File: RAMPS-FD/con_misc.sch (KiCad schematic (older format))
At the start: 15 parts, among them K201 S1, K202 S2, K203 S3, K204 S4, P1 SERIAL1, P2 I2C-1, P211 I2C-0, P213 AUX-4, P214 AUX-2, P215 AUX-3, P216 SERIAL0

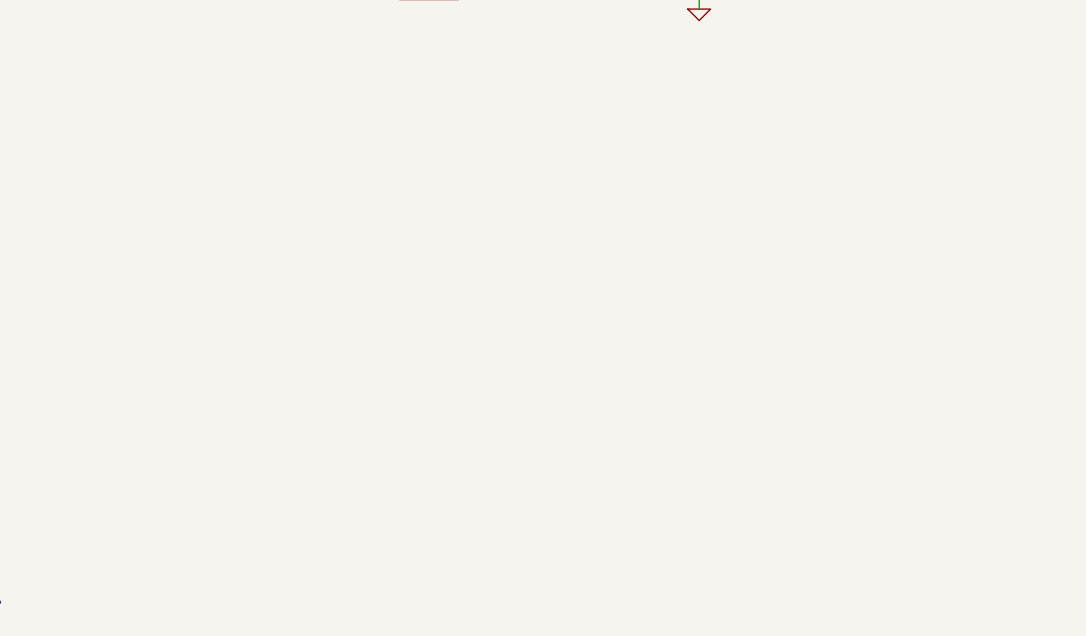
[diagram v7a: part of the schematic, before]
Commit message: RAMPS-FD schematic changes: #3 replace C301, C302, C303 and C501 with ceramic 0805; #4 change endstop connectors to 6x1 and 6x2 to allow key position #9 change E-STOP connector to KK type; #18 add 10k pulldowns on heater outputs from CPU #19 change E-STOP buffers to HCT type to always drive FETs at 5V and remove inverting drivers on heater outputs; #20 add 24LC256 I2C EEPROM
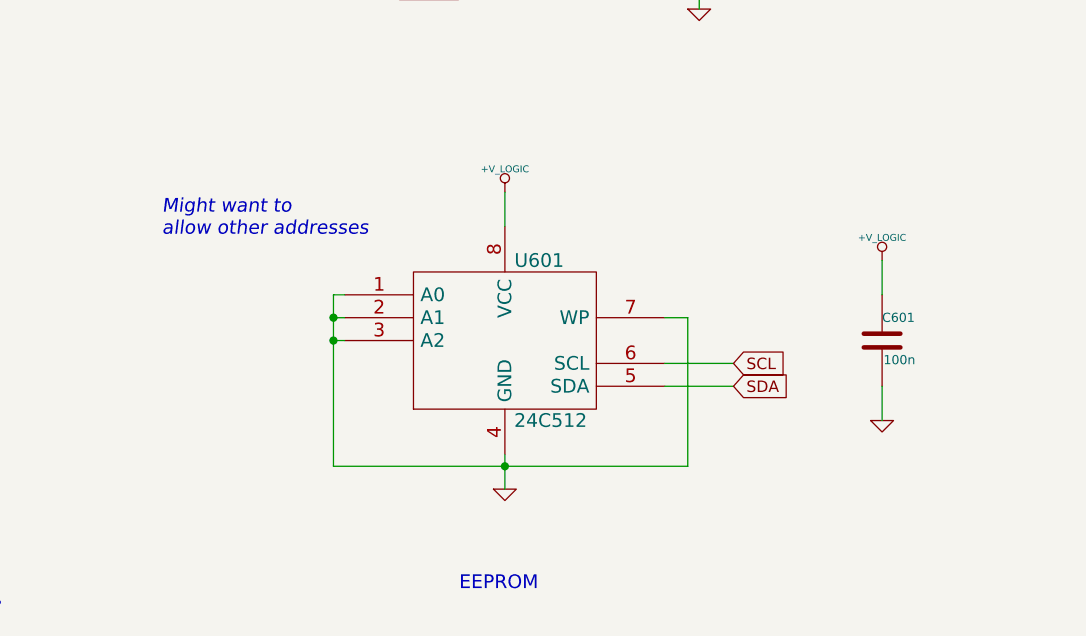
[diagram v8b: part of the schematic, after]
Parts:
- added C601: 100n, ~, symbol C
- added U601: 24C512, symbol 24C512
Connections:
- net +V_LOGIC: now also C601.1, U601.8 (VCC)
- net GND: now also C601.2, U601.1 (A0), U601.2 (A1), U601.3 (A2), U601.4 (GND), U601.7 (WP)
- net SCL: now also U601.6 (SCL)
- net SDA: now also U601.5 (SDA)
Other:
- note added: "EEPROM"
- note added: "Might want to \nallow other addresses"
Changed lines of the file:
@@
 Sheet 6 9
 Title ""
-Date "6 oct 2013"
+Date "18 dec 2013"
 Rev "0.2"
 Comp ""
@@
 $EndComp
 $Comp
-L GND #PWR065
+L GND #PWR067
 U 1 1 523B601D
 P 5250 4800
-F 0 "#PWR065" H 5250 4800 30  0001 C CNN
+F 0 "#PWR067" H 5250 4800 30  0001 C CNN
 F 1 "GND" H 5250 4730 30  0001 C CNN
 F 2 "" H 5250 4800 60  0001 C CNN
@@
 SCL1
 $Comp
-L +V_LOGIC #PWR066
+L +V_LOGIC #PWR068
 U 1 1 523B601C
 P 4450 3800
-F 0 "#PWR066" H 4450 3770 30  0001 C CNN
+F 0 "#PWR068" H 4450 3770 30  0001 C CNN
 F 1 "+V_LOGIC" H 4450 3900 30  0000 C CNN
 F 2 "" H 4450 3800 60  0001 C CNN
@@
 UART1_TX_LV
 $Comp
-L GND #PWR067
+L GND #PWR069
 U 1 1 523B5AB9
 P 1950 3600
-F 0 "#PWR067" H 1950 3600 30  0001 C CNN
+F 0 "#PWR069" H 1950 3600 30  0001 C CNN
 F 1 "GND" H 1950 3530 30  0001 C CNN
 F 2 "" H 1950 3600 60  0001 C CNN
@@
 D51-MOSI
 $Comp
-L +V_LOGIC #PWR068
+L +V_LOGIC #PWR070
 U 1 1 517867DD
 P 7950 1750
-F 0 "#PWR068" H 7950 1720 30  0001 C CNN
+F 0 "#PWR070" H 7950 1720 30  0001 C CNN
 F 1 "+V_LOGIC" H 7950 1850 30  0000 C CNN
 F 2 "" H 7950 1750 60  0001 C CNN
@@
 $EndComp
 $Comp
-L +V_LOGIC #PWR069
+L +V_LOGIC #PWR071
 U 1 1 517867D0
 P 8250 6850
-F 0 "#PWR069" H 8250 6820 30  0001 C CNN
+F 0 "#PWR071" H 8250 6820 30  0001 C CNN
 F 1 "+V_LOGIC" H 8250 6950 30  0000 C CNN
 F 2 "" H 8250 6850 60  0001 C CNN
@@
 $EndComp
 $Comp
-L +V_LOGIC #PWR070
+L +V_LOGIC #PWR072
 U 1 1 517867C6
 P 4450 1600
-F 0 "#PWR070" H 4450 1570 30  0001 C CNN
+F 0 "#PWR072" H 4450 1570 30  0001 C CNN
 F 1 "+V_LOGIC" H 4450 1700 30  0000 C CNN
 F 2 "" H 4450 1600 60  0001 C CNN
@@
 $EndComp
 $Comp
-L GND #PWR071
+L GND #PWR073
 U 1 1 51084B2C
 P 9100 6800
-F 0 "#PWR071" H 9100 6800 30  0001 C CNN
+F 0 "#PWR073" H 9100 6800 30  0001 C CNN
 F 1 "GND" H 9100 6730 30  0001 C CNN
 F 2 "" H 9100 6800 60  0001 C CNN
@@
 Must not have external pullups to 5V if IOREF = 3.3V
 $Comp
-L GND #PWR072
+L GND #PWR074
 U 1 1 5104884C
 P 7550 3600
-F 0 "#PWR072" H 7550 3600 30  0001 C CNN
+F 0 "#PWR074" H 7550 3600 30  0001 C CNN
 F 1 "GND" H 7550 3530 30  0001 C CNN
 F 2 "" H 7550 3600 60  0001 C CNN
@@
 $EndComp
 $Comp
-L GND #PWR073
+L GND #PWR075
 U 1 1 51048839
 P 10000 1900
-F 0 "#PWR073" H 10000 1900 30  0001 C CNN
+F 0 "#PWR075" H 10000 1900 30  0001 C CNN
 F 1 "GND" H 10000 1830 30  0001 C CNN
 F 2 "" H 10000 1900 60  0001 C CNN
@@
 $EndComp
 $Comp
-L GND #PWR074
+L GND #PWR076
 U 1 1 5104861F
 P 1950 2350
-F 0 "#PWR074" H 1950 2350 30  0001 C CNN
+F 0 "#PWR076" H 1950 2350 30  0001 C CNN
 F 1 "GND" H 1950 2280 30  0001 C CNN
 F 2 "" H 1950 2350 60  0001 C CNN
@@
 $EndComp
 $Comp
-L GND #PWR075
+L GND #PWR077
 U 1 1 51047C7E
 P 1550 6850
-F 0 "#PWR075" H 1550 6850 30  0001 C CNN
+F 0 "#PWR077" H 1550 6850 30  0001 C CNN
 F 1 "GND" H 1550 6780 30  0001 C CNN
 F 2 "" H 1550 6850 60  0001 C CNN
@@
 $EndComp
 $Comp
-L +5V #PWR076
+L +5V #PWR078
 U 1 1 51047C7D
 P 1550 6450
-F 0 "#PWR076" H 1550 6540 20  0001 C CNN
+F 0 "#PWR078" H 1550 6540 20  0001 C CNN
 F 1 "+5V" H 1550 6540 30  0000 C CNN
 F 2 "" H 1550 6450 60  0001 C CNN
@@
 SERVO3
 $Comp
-L +5V #PWR077
+L +5V #PWR079
 U 1 1 51047C7B
 P 1550 5700
-F 0 "#PWR077" H 1550 5790 20  0001 C CNN
+F 0 "#PWR079" H 1550 5790 20  0001 C CNN
 F 1 "+5V" H 1550 5790 30  0000 C CNN
 F 2 "" H 1550 5700 60  0001 C CNN
@@
 $EndComp
 $Comp
-L GND #PWR078
+L GND #PWR080
 U 1 1 51047C7A
 P 1550 6100
-F 0 "#PWR078" H 1550 6100 30  0001 C CNN
+F 0 "#PWR080" H 1550 6100 30  0001 C CNN
 F 1 "GND" H 1550 6030 30  0001 C CNN
 F 2 "" H 1550 6100 60  0001 C CNN
@@
 $EndComp
 $Comp
-L GND #PWR079
+L GND #PWR081
 U 1 1 51047C77
 P 1550 5450
-F 0 "#PWR079" H 1550 5450 30  0001 C CNN
+F 0 "#PWR081" H 1550 5450 30  0001 C CNN
 F 1 "GND" H 1550 5380 30  0001 C CNN
 F 2 "" H 1550 5450 60  0001 C CNN
@@
 $EndComp
 $Comp
-L +5V #PWR080
+L +5V #PWR082
 U 1 1 51047C76
 P 1550 5050
-F 0 "#PWR080" H 1550 5140 20  0001 C CNN
+F 0 "#PWR082" H 1550 5140 20  0001 C CNN
 F 1 "+5V" H 1550 5140 30  0000 C CNN
 F 2 "" H 1550 5050 60  0001 C CNN
@@
 SERVO1
 $Comp
-L +5V #PWR081
+L +5V #PWR083
 U 1 1 51047C09
 P 1550 4300
-F 0 "#PWR081" H 1550 4390 20  0001 C CNN
+F 0 "#PWR083" H 1550 4390 20  0001 C CNN
 F 1 "+5V" H 1550 4390 30  0000 C CNN
 F 2 "" H 1550 4300 60  0001 C CNN
@@
 $EndComp
 $Comp
-L GND #PWR082
+L GND #PWR084
 U 1 1 51047C01
 P 1550 4700
-F 0 "#PWR082" H 1550 4700 30  0001 C CNN
+F 0 "#PWR084" H 1550 4700 30  0001 C CNN
 F 1 "GND" H 1550 4630 30  0001 C CNN
 F 2 "" H 1550 4700 60  0001 C CNN
@@
 SDA
 $Comp
-L GND #PWR083
+L GND #PWR085
 U 1 1 51047413
 P 5250 2600
-F 0 "#PWR083" H 5250 2600 30  0001 C CNN
+F 0 "#PWR085" H 5250 2600 30  0001 C CNN
 F 1 "GND" H 5250 2530 30  0001 C CNN
 F 2 "" H 5250 2600 60  0001 C CNN
@@
 	9400 6100 8050 6100
 $Comp
-L +5V #PWR084
+L +5V #PWR086
 U 1 1 52421C84
 P 7950 3100
-F 0 "#PWR084" H 7950 3190 20  0001 C CNN
+F 0 "#PWR086" H 7950 3190 20  0001 C CNN
 F 1 "+5V" H 7950 3190 30  0000 C CNN
 F 2 "" H 7950 3100 60  0000 C CNN
@@
 $EndComp
 $Comp
-L +V_LOGIC #PWR085
+L +V_LOGIC #PWR087
 U 1 1 52475621
 P 10250 3650
-F 0 "#PWR085" H 10250 3620 30  0001 C CNN
+F 0 "#PWR087" H 10250 3620 30  0001 C CNN
 F 1 "+V_LOGIC" H 10250 3750 30  0000 C CNN
 F 2 "" H 10250 3650 60  0001 C CNN
@@
 Text Notes 10100 3150 0    60   ~ 0
 Note: Some addon boards \nconnect this pin to GND.
+$Comp
+L 24C512 U601
+U 1 1 52B23647
+P 4400 6250
+F 0 "U601" H 4550 6600 60  0000 C CNN
+F 1 "24C512" H 4600 5900 60  0000 C CNN
+F 2 "" H 4400 6250 60  0000 C CNN
+F 3 "" H 4400 6250 60  0000 C CNN
+	1    4400 6250
+	1    0    0    -1
+$EndComp
+$Comp
+L GND #PWR088
+U 1 1 52B23654
+P 4400 6900
+F 0 "#PWR088" H 4400 6900 30  0001 C CNN
+F 1 "GND" H 4400 6830 30  0001 C CNN
+F 2 "" H 4400 6900 60  0001 C CNN
+F 3 "" H 4400 6900 60  0001 C CNN
+	1    4400 6900
+	1    0    0    -1
+$EndComp
+Wire Wire Line
+	4400 6750 4400 6900
+Wire Wire Line
+	3650 6250 3700 6250
+Wire Wire Line
+	3650 6050 3650 6800
+Wire Wire Line
+	3650 6800 5200 6800
+Connection ~ 4400 6800
+Wire Wire Line
+	3650 6150 3700 6150
+Connection ~ 3650 6250
+Wire Wire Line
+	3700 6050 3650 6050
+Connection ~ 3650 6150
+$Comp
+L +V_LOGIC #PWR089
+U 1 1 52B2384C
+P 4400 5600
+F 0 "#PWR089" H 4400 5570 30  0001 C CNN
+F 1 "+V_LOGIC" H 4400 5700 30  0000 C CNN
+F 2 "" H 4400 5600 60  0001 C CNN
+F 3 "" H 4400 5600 60  0001 C CNN
+	1    4400 5600
+	1    0    0    -1
+$EndComp
+Wire Wire Line
+	4400 5750 4400 5600
+Wire Wire Line
+	5100 6150 5200 6150
+Wire Wire Line
+	5200 6150 5200 6800
+Text GLabel 5400 6350 2    50   Input ~ 0
+SCL
+Text GLabel 5400 6450 2    50   Input ~ 0
+SDA
+Wire Wire Line
+	5100 6450 5400 6450
+Wire Wire Line
+	5100 6350 5400 6350
+Text Notes 4200 7350 0    60   ~ 0
+EEPROM
+$Comp
+L C C601
+U 1 1 52B22339
+P 6050 6250
+F 0 "C601" H 6050 6350 40  0000 L CNN
+F 1 "100n" H 6056 6165 40  0000 L CNN
+F 2 "~" H 6088 6100 30  0000 C CNN
+F 3 "~" H 6050 6250 60  0000 C CNN
+	1    6050 6250
+	1    0    0    -1
+$EndComp
+$Comp
+L GND #PWR090
+U 1 1 52B22346
+P 6050 6600
+F 0 "#PWR090" H 6050 6600 30  0001 C CNN
+F 1 "GND" H 6050 6530 30  0001 C CNN
+F 2 "" H 6050 6600 60  0001 C CNN
+F 3 "" H 6050 6600 60  0001 C CNN
+	1    6050 6600
+	1    0    0    -1
+$EndComp
+Wire Wire Line
+	6050 6450 6050 6600
+$Comp
+L +V_LOGIC #PWR091
+U 1 1 52B2234D
+P 6050 5900
+F 0 "#PWR091" H 6050 5870 30  0001 C CNN
+F 1 "+V_LOGIC" H 6050 6000 30  0000 C CNN
+F 2 "" H 6050 5900 60  0001 C CNN
+F 3 "" H 6050 5900 60  0001 C CNN
+	1    6050 5900
+	1    0    0    -1
+$EndComp
+Wire Wire Line
+	6050 6050 6050 5900
+Text Notes 2900 5800 0    60   Italic 0
+Might want to \nallow other addresses
 $EndSCHEMATC
